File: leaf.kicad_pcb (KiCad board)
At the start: 6 copper layers, 49.8 x 49.7 mm, 292 parts, among them J1 Micro_SD_Card_Det1, J2 MIPI-CSI, J3 USB_OTG, Q1 Q_PNP_BEC, SW1 SKSGPAE010, SW2 SKSGPAE010, U1 BL8039, U2 rv1126/rv1109, U3 MTFC4GACAJCN, U4 AP6526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

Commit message: updated routes
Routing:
- net /DDR/DDR4_A14_~{WE}: track 42.6 -> 37.3 mm
- net /DDR/DDR4_ODT0: track 39.2 -> 38.7 mm

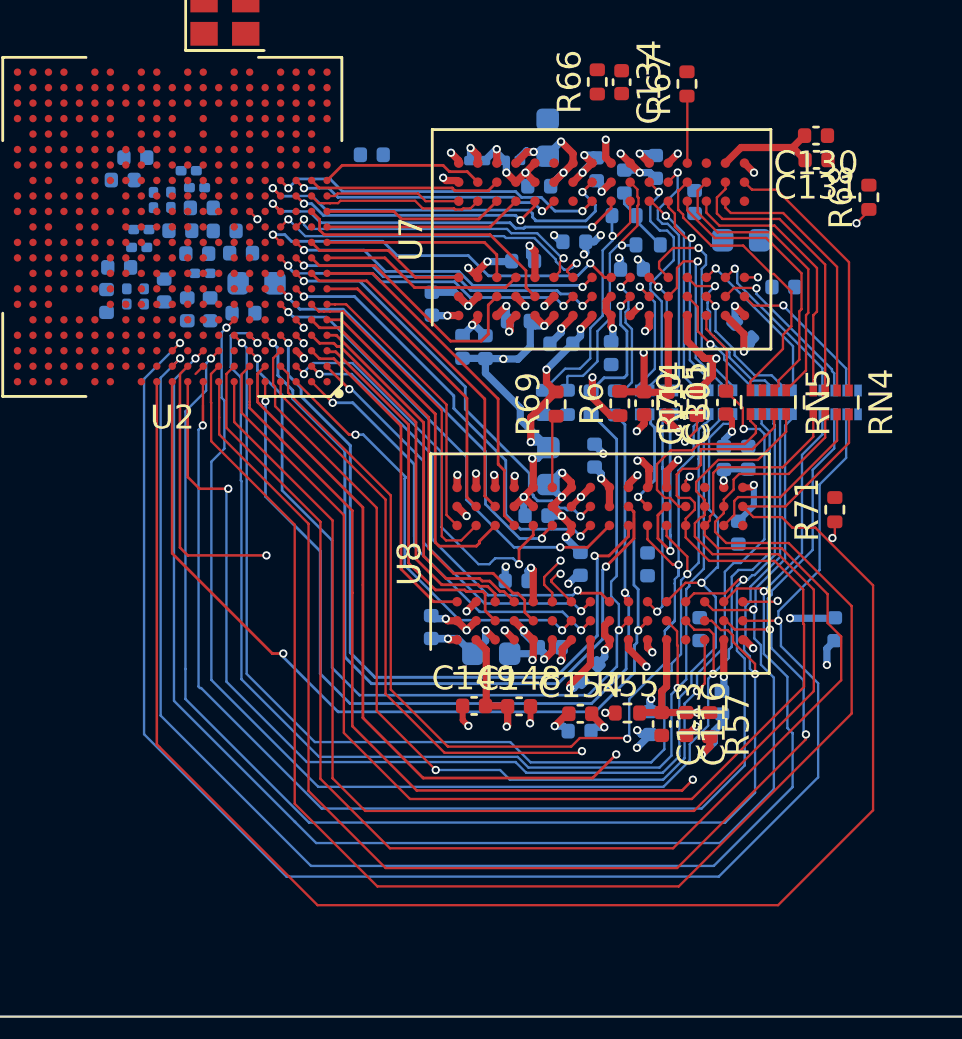
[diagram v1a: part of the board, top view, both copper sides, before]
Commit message: routing DDR
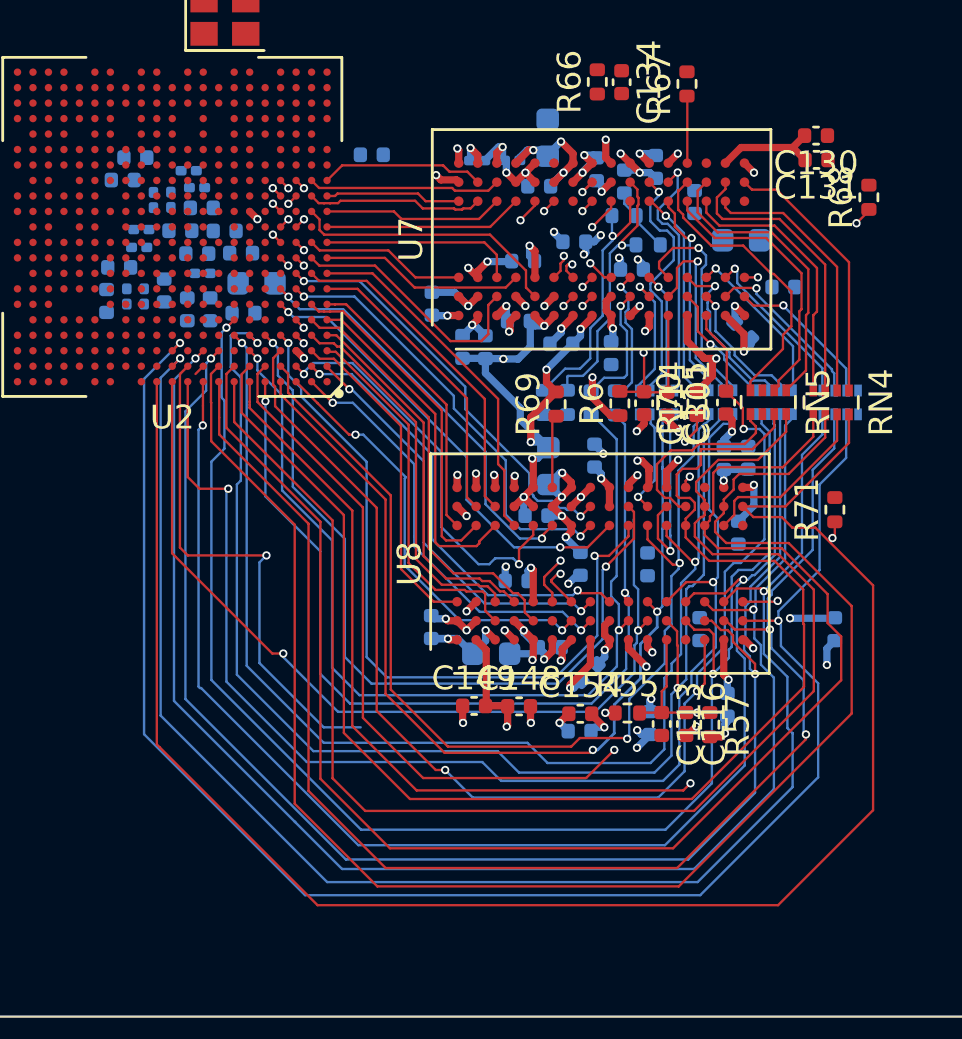
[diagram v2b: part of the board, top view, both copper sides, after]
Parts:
- moved C157 0.24 mm to (164.0, 99.6)
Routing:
- net /DDR/DDR4_A16_~{RAS}: track 16.0 -> 26.0 mm
- net /DDR/DDR4_~{ACT}: track 33.3 -> 40.8 mm
- net /DDR/DDR4_DM0: track 10.9 -> 16.1 mm
- net /DDR/DDR4_D1: track 13.4 -> 17.6 mm
- net /DDR/DDR4_BA0: track 57.6 -> 60.2 mm
- net GND: track 83.7 -> 82.3 mm
- net /DDR/DDR4_A6: track 62.0 -> 63.3 mm
- net /DDR/DDR4_A4: track 57.3 -> 58.6 mm
- net /DDR/DDR4_~{CS0}: track 44.9 -> 43.9 mm
- net /DDR/DDR_~{RESET}: track 55.4 -> 56.4 mm
- net /DDR/DDR4_A0: track 62.9 -> 63.8 mm
- net /DDR/DDR4_D7: track 11.5 -> 12.3 mm
- net /DDR/DDR4_D2: track 14.1 -> 14.8 mm
- net /DDR/DDR4_A11: track 68.6 -> 69.3 mm
- net /DDR/DDR4_A2: track 65.5 -> 66.1 mm
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
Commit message: updated PCB
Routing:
- net /DDR/DDR4_D1: track 17.6 -> 16.2 mm
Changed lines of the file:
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@@
   (via (at 157.12815 82.875) (size 0.35) (drill 0.2) (layers "F.Cu" "B.Cu") (net 172))
   (via (at 145.56815 81.18) (size 0.35) (drill 0.2) (layers "F.Cu" "B.Cu") (net 172))
-  (segment (start 151.554186 84.58) (end 155.02 84.58) (width 0.116078) (layer "In3.Cu") (net 172))
+  (segment (start 156.71315 83.29) (end 157.12815 82.875) (width 0.116078) (layer "In3.Cu") (net 172))
+  (segment (start 145.99 82.18) (end 146.83 82.18) (width 0.116078) (layer "In3.Cu") (net 172))
   (segment (start 155.57 83.54) (end 155.82 83.29) (width 0.116078) (layer "In3.Cu") (net 172))
-  (segment (start 149.995736 84.28) (end 149.995736 83.938187) (width 0.116078) (layer "In3.Cu") (net 172))
-  (segment (start 156.71315 83.29) (end 157.12815 82.875) (width 0.116078) (layer "In3.Cu") (net 172))
-  (segment (start 150.595736 83.938187) (end 150.595736 84.28) (width 0.116078) (layer "In3.Cu") (net 172))
   (segment (start 145.56815 81.18) (end 145.56815 81.75815) (width 0.116078) (layer "In3.Cu") (net 172))
+  (segment (start 155.57 84.03) (end 155.57 83.54) (width 0.116078) (layer "In3.Cu") (net 172))
+  (segment (start 145.56815 81.75815) (end 145.99 82.18) (width 0.116078) (layer "In3.Cu") (net 172))
+  (segment (start 147.15 82.5) (end 147.15 83.95) (width 0.116078) (layer "In3.Cu") (net 172))
+  (segment (start 146.83 82.18) (end 147.15 82.5) (width 0.116078) (layer "In3.Cu") (net 172))
   (segment (start 155.02 84.58) (end 155.57 84.03) (width 0.116078) (layer "In3.Cu") (net 172))
   (segment (start 155.82 83.29) (end 156.71315 83.29) (width 0.116078) (layer "In3.Cu") (net 172))
   (segment (start 147.15 83.95) (end 147.78 84.58) (width 0.116078) (layer "In3.Cu") (net 172))
-  (segment (start 155.57 84.03) (end 155.57 83.54) (width 0.116078) (layer "In3.Cu") (net 172))
-  (segment (start 147.15 82.5) (end 147.15 83.95) (width 0.116078) (layer "In3.Cu") (net 172))
-  (segment (start 146.83 82.18) (end 147.15 82.5) (width 0.116078) (layer "In3.Cu") (net 172))
-  (segment (start 150.895736 84.58) (end 151.554186 84.58) (width 0.116078) (layer "In3.Cu") (net 172))
-  (segment (start 147.78 84.58) (end 149.695736 84.58) (width 0.116078) (layer "In3.Cu") (net 172))
-  (segment (start 145.99 82.18) (end 146.83 82.18) (width 0.116078) (layer "In3.Cu") (net 172))
-  (segment (start 145.56815 81.75815) (end 145.99 82.18) (width 0.116078) (layer "In3.Cu") (net 172))
-  (arc (start 149.995736 83.938187) (mid 150.083604 83.726055) (end 150.295736 83.638187) (width 0.116078) (layer "In3.Cu") (net 172))
-  (arc (start 150.295736 83.638187) (mid 150.507868 83.726055) (end 150.595736 83.938187) (width 0.116078) (layer "In3.Cu") (net 172))
-  (arc (start 150.595736 84.28) (mid 150.683604 84.492132) (end 150.895736 84.58) (width 0.116078) (layer "In3.Cu") (net 172))
-  (arc (start 149.695736 84.58) (mid 149.907868 84.492132) (end 149.995736 84.28) (width 0.116078) (layer "In3.Cu") (net 172))
+  (segment (start 147.78 84.58) (end 155.02 84.58) (width 0.116078) (layer "In3.Cu") (net 172))
   (segment (start 145.56815 81.18) (end 145.56815 81.235) (width 0.1) (layer "B.Cu") (net 172))
   (segment (start 153.80815 80.205) (end 154.32815 80.725) (width 0.1) (layer "F.Cu") (net 173))
@@
   (segment (start 169.29315 79.4) (end 167.02315 81.67) (width 0.1) (layer "In3.Cu") (net 522))
   (segment (start 167.02315 81.67) (end 165.29315 81.67) (width 0.1) (layer "In3.Cu") (net 522))
-  (generated (id 6235da5c-2304-40f2-93d2-017416e4db83)
-    (type tuning_pattern) (name "Tuning Pattern")
-    (layer "In3.Cu")
-    (base_line (pts
-      (xy 149.695736 84.58)
-      (xy 151.554186 84.58)
-    ))
-    (corner_radius_percent 100)
-    (end (xy 151.554186 84.58))
-    (initial_side "left")
-    (last_diff_pair_gap 0.18)
-    (last_netname "/DDR/DDR4_D1")
-    (last_status "tuned")
-    (last_track_width 0.155)
-    (last_tuning "650.32 mils (tuned)")
-    (max_amplitude 1)
-    (min_spacing 0.6)
-    (origin (xy 149.695736 84.58))
-    (override_custom_rules yes)
-    (rounded yes)
-    (single_sided no)
-    (target_length 16.518128)
-    (target_length_max 16.618128)
-    (target_length_min 16.418128)
-    (target_skew 0)
-    (target_skew_max 0.1)
-    (target_skew_min -0.1)
-    (tuning_mode "single")
-    (members
-      22b584e3-80b6-482c-8887-fa93f992a302
-      23704880-690f-4bd9-b7de-b4e611ced2cc
-      37a6eec8-4271-4fbd-a2a7-342e50313a01
-      8fd3e2fb-c7cc-46d8-b528-c9f50c801b5e
-      b67bd3f9-4fac-43a0-9ffd-bbb8979d45c0
-      c01a50a8-ca15-4fa0-973b-fe8ed034240e
-      d9c7a4f3-0a12-4d6c-a495-2583b9b20bbc
-    )
-  )
   (generated (id 90b95dc0-62d4-4c0c-b33b-2a12cf9867a7)
     (type tuning_pattern) (name "Tuning Pattern")

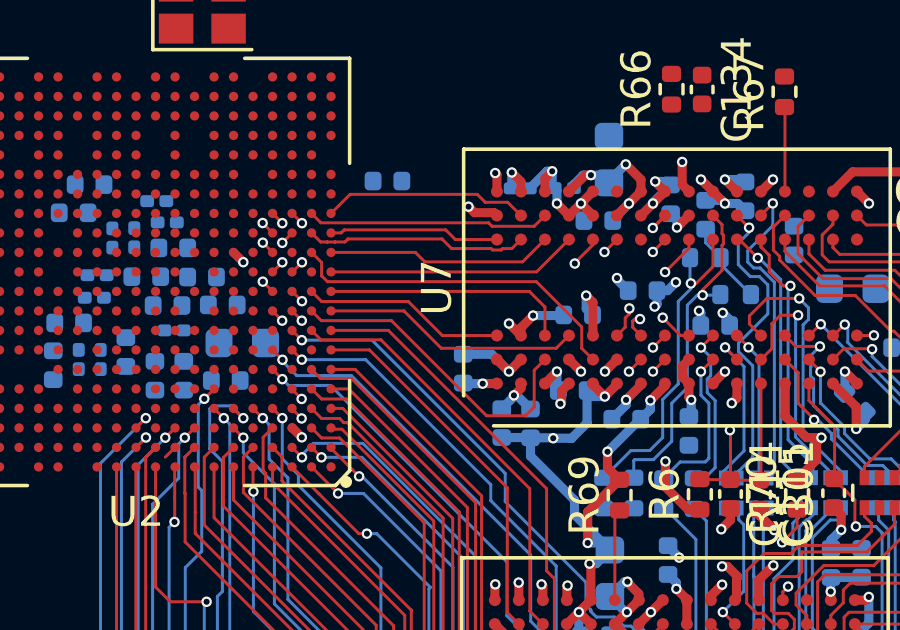
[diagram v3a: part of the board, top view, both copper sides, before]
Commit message: length tuning on DDR Data 0 bus
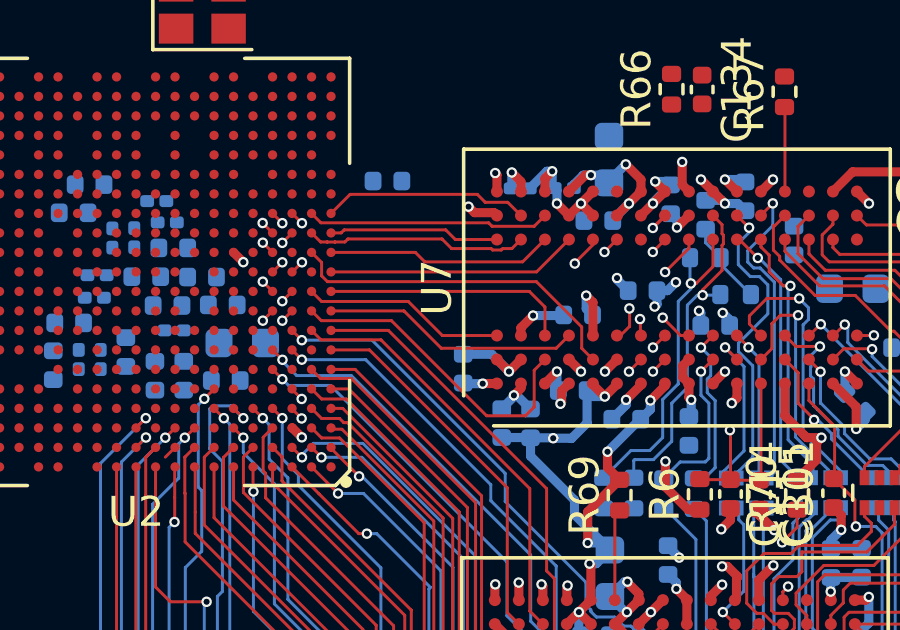
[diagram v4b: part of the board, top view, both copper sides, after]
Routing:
- net /DDR/DDR4_D5: track 13.4 -> 18.9 mm
- net /DDR/DDR4_D4: track 13.7 -> 18.2 mm
- net /DDR/DDR4_D7: track 12.3 -> 15.2 mm
- net /DDR/DDR4_DQS0N: track 13.3 -> 15.2 mm
- net /DDR/DDR4_D2: track 14.8 -> 16.4 mm
- net /DDR/DDR4_DQS0P: track 14.0 -> 15.2 mm
- net VCC_DDR: track 57.7 -> 57.1 mm, vias 44 -> 43

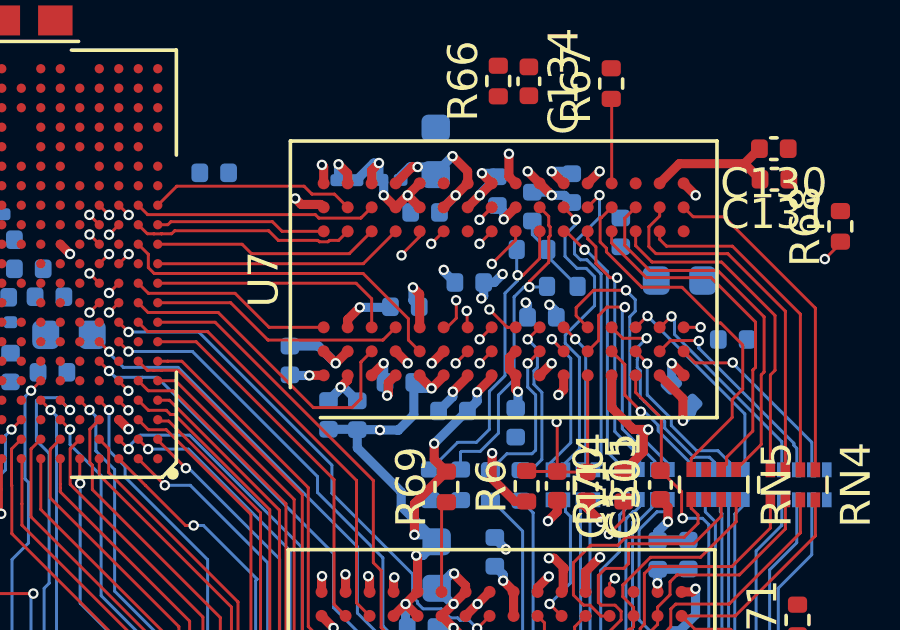
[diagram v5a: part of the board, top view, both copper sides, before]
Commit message: tuning length of DDR Data 0 bus
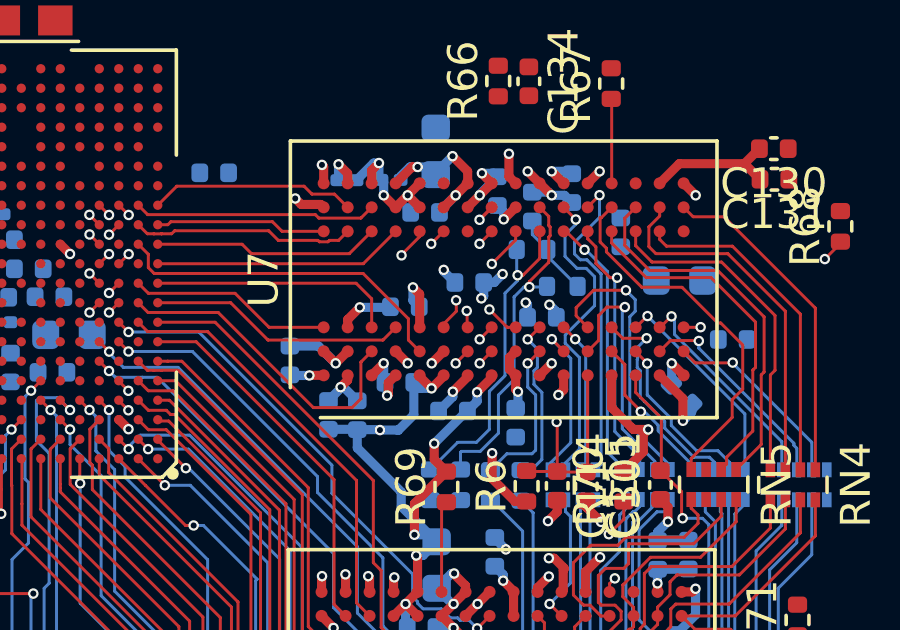
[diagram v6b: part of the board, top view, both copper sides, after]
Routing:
- net /DDR/DDR4_D6: track 16.5 -> 18.4 mm

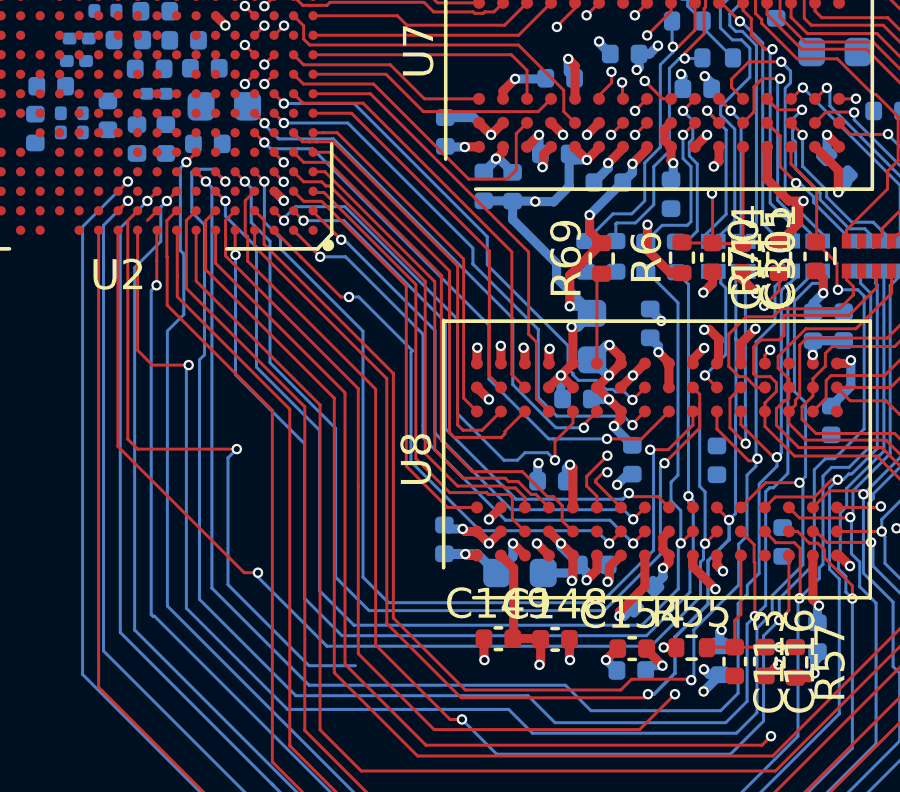
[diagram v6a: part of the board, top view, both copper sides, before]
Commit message: tuned DDR CLK traces
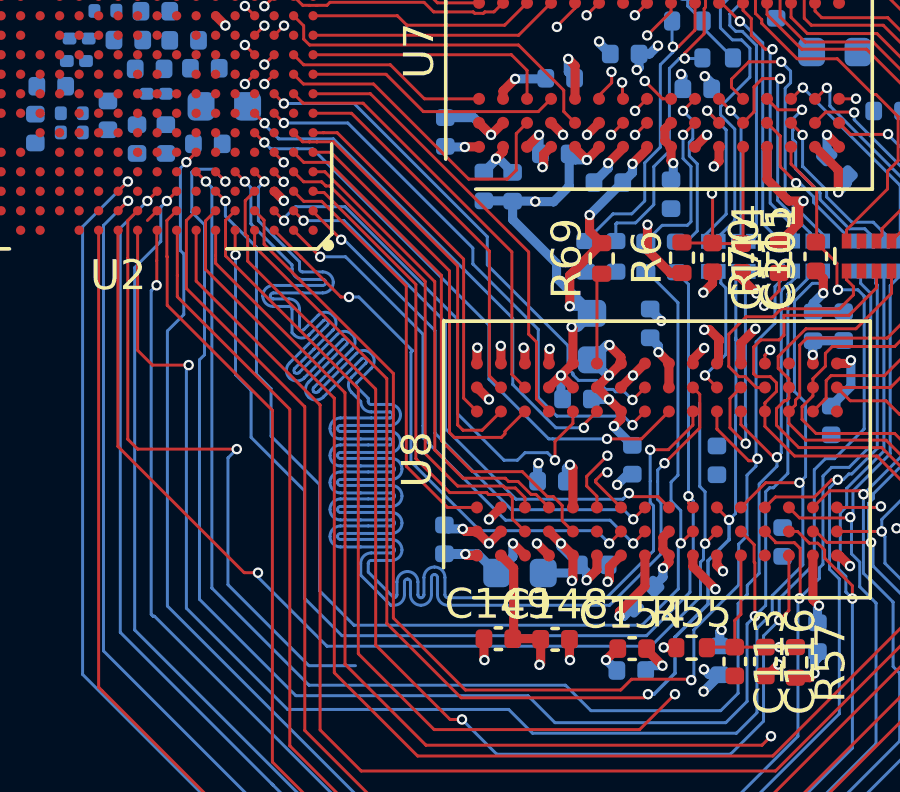
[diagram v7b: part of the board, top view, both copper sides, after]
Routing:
- net /DDR/DDR4_CLK_P: track 31.4 -> 68.7 mm
- net /DDR/DDR4_CLK_N: track 33.2 -> 70.1 mm

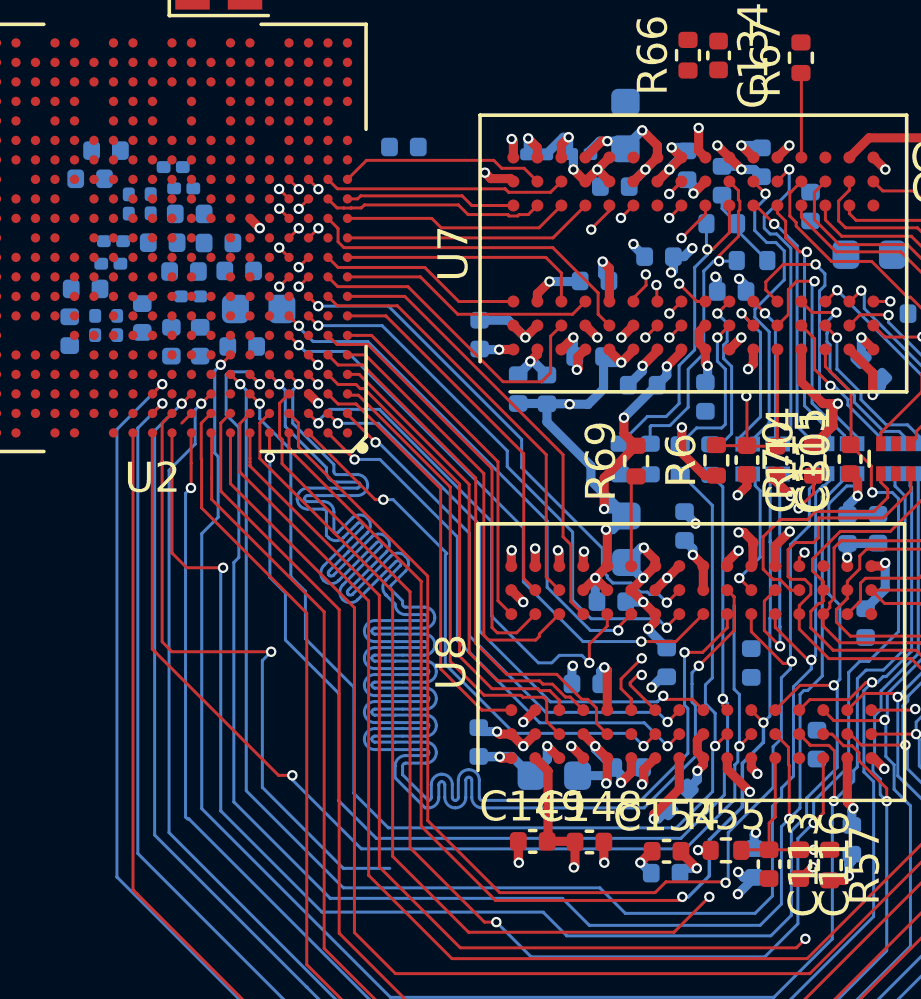
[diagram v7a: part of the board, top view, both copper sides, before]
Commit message: routed DDR CLK_B
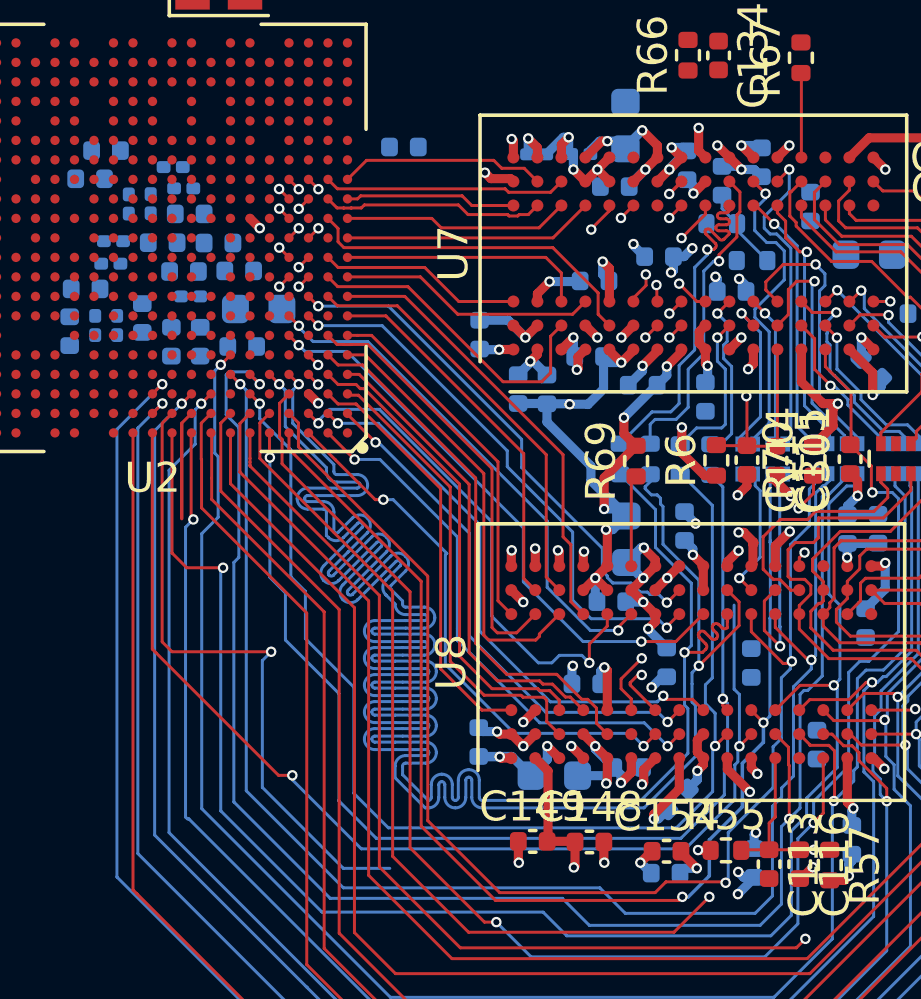
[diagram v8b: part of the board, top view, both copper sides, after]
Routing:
- net /DDR/DDR4_CLK_P: track 68.7 -> 77.1 mm
- net /DDR/DDR4_CLK_N: track 70.1 -> 77.5 mm
- net /DDR/DDR4_A9: track 8.14 -> 11.3 mm
- net /DDR/DDR Chips/DDR4_CLK_B_P: track 10.8 -> 12.4 mm
- net /DDR/DDR Chips/DDR4_CLK_B_N: track 11.2 -> 10.7 mm
